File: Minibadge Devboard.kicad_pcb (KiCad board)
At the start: 2 copper layers, 30.5 x 48.3 mm, 39 parts, among them Q1 PMOS, SW1 Power, SW3 SPEED, SW4 NTC, U1 DRV8837C, U2 74HC4060

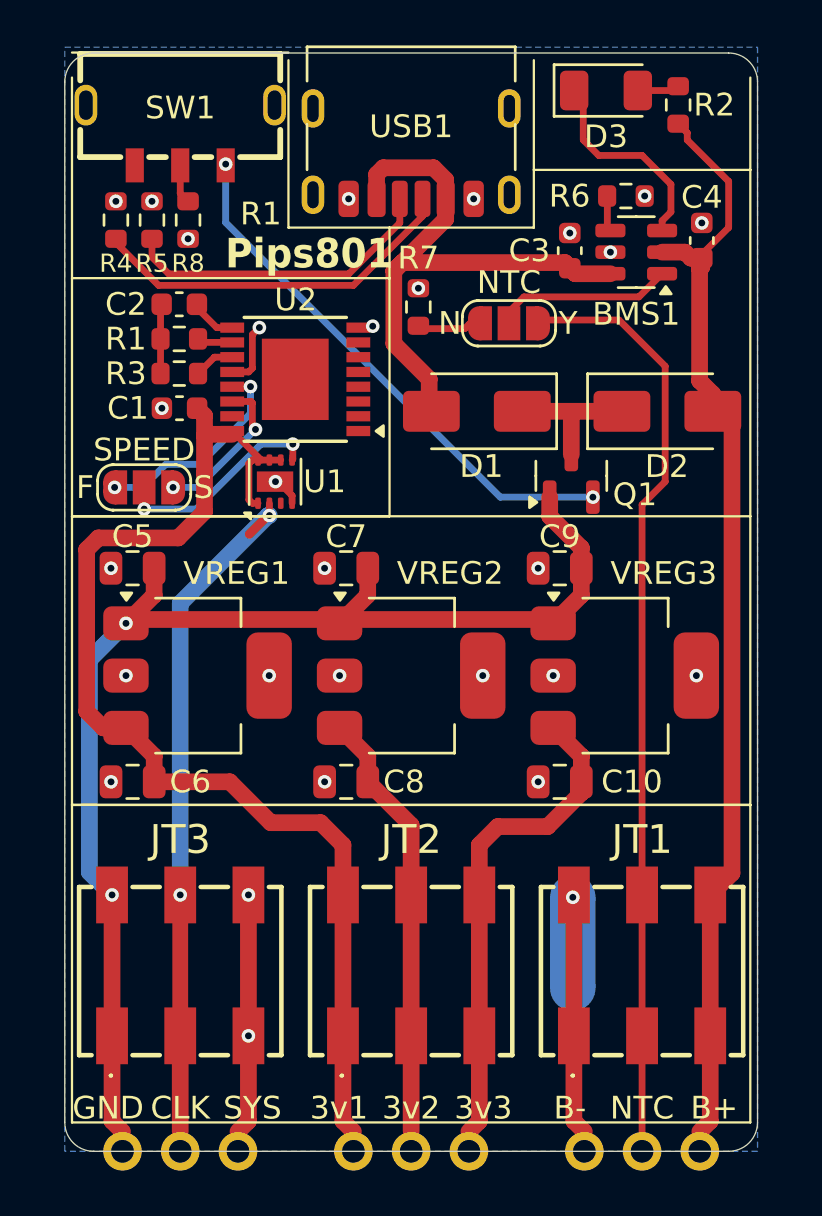
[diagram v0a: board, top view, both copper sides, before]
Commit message: Add Footprint and Symbol
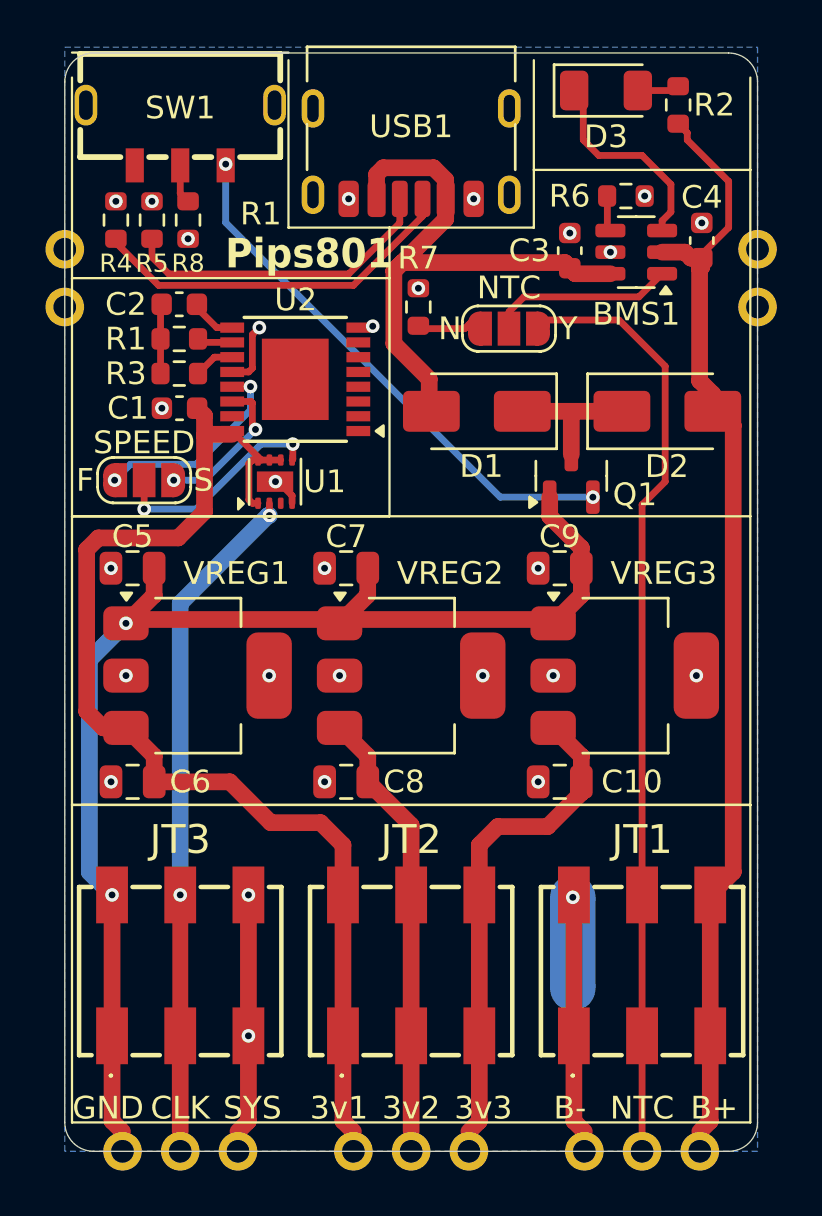
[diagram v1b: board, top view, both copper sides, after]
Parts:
- added G***: LOGO, LOGO, B.Cu at (178.8, 116.8)
- added REF**: Castellated pins 1x02, Castellated pins:Castellated pins 1x02, F.Cu at (195.6, 105.1)
- added REF**: Castellated pins 1x02, Castellated pins:Castellated pins 1x02, F.Cu at (165.1, 105.1)
- moved SW3 0.32 mm to (168.6, 112.7)
- moved SW4 0.24 mm to (184.6, 106.0)
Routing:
- net CLK: track 30.5 -> 29.4 mm

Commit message: Silkscreen fixes and thermal via stitching/anchoring
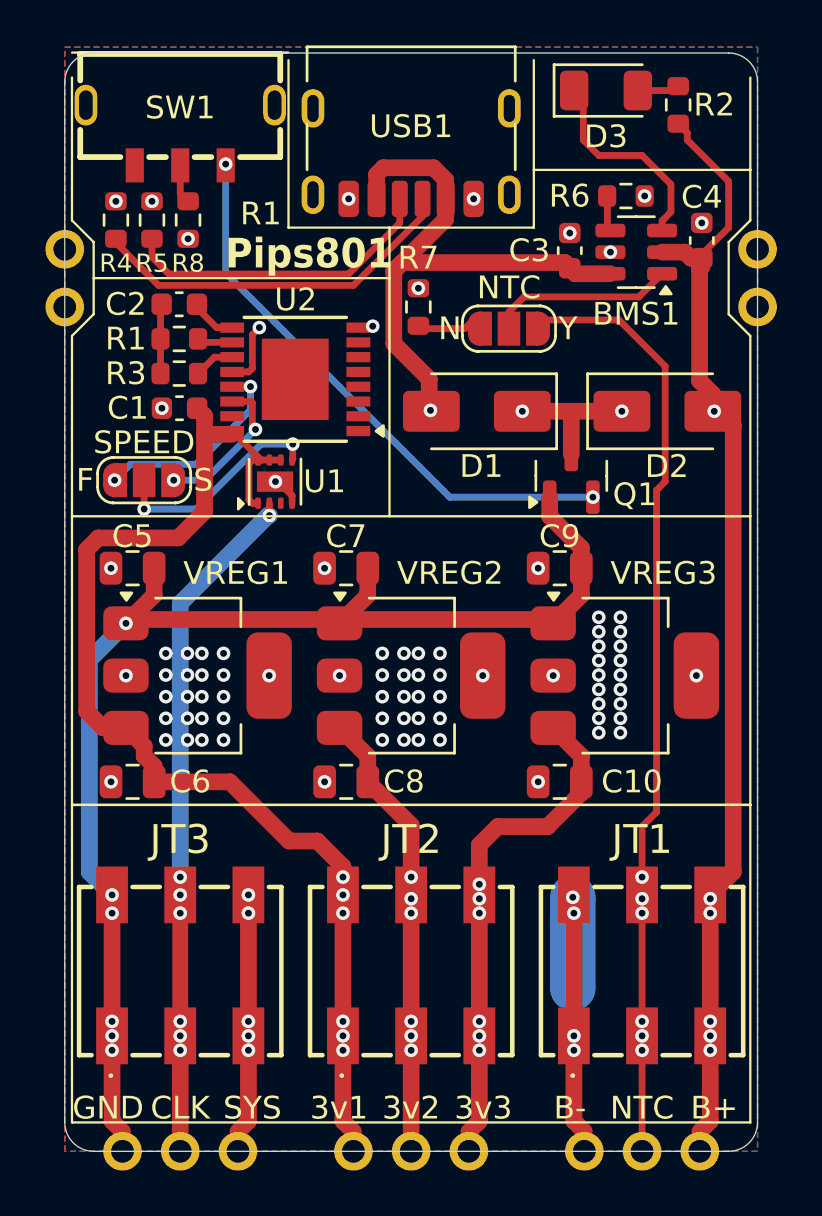
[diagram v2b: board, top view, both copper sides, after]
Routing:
- net Net-(Q1-G): track 23.7 -> 25.0 mm
- net +3.3V-1: track 51.3 -> 50.7 mm, vias 0 -> 6
- net VBUS: vias 0 -> 1
- net GND: vias 28 -> 89
- net VDD: vias 0 -> 2
- net SYS: vias 2 -> 6
- net NTC: vias 0 -> 6
- net CLK: vias 2 -> 7
- net -BATT: vias 1 -> 4
- net +BATT: vias 0 -> 6
- net +3.3V-3: vias 0 -> 6
- net +3.3V-2: vias 0 -> 6
- added copper zone on F.Cu, net GND

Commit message: Add support for external PSU and Power switch
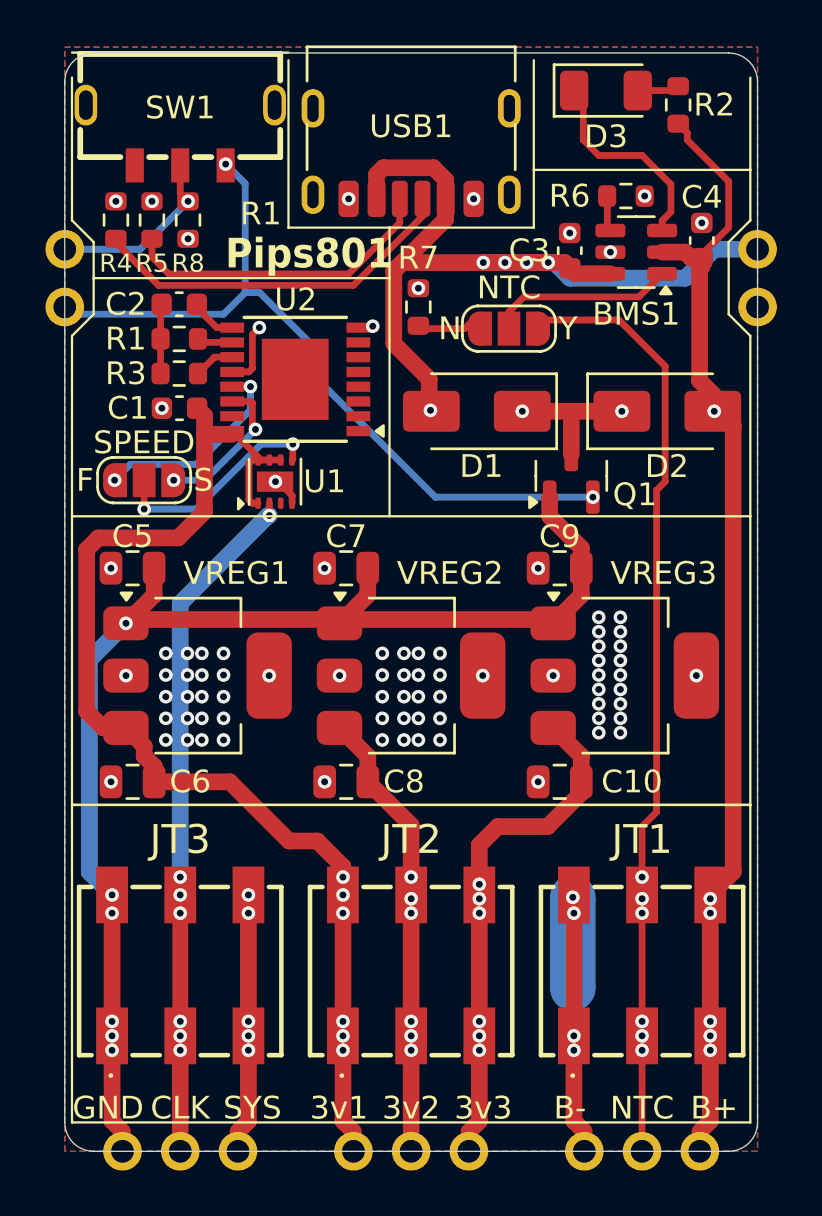
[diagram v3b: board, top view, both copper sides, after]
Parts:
- D3: value Charge -> RED
- J1: renamed from REF**; value Castellated pins 1x02 -> External power
- J2: renamed from REF**; value Castellated pins 1x02 -> External switch
- R1: value 8.45k -> 8.45kΩ
- R3: value 20k -> 20kΩ
- R4, R5: value 5.1k -> 5.1kΩ
- R6: value 675 -> 675Ω
- R7: value 10k -> 10kΩ
- R8: value 100k -> 100kΩ
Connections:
- J1 pad 1: (no net) -> GND
- J1 pad 2: (no net) -> VBUS
- J2 pad 1: (no net) -> SW1
- J2 pad 2: (no net) -> SW2
- Q1 pad 2: Net-(Q1-G) -> SW1
- R8 pad 1: Net-(SW1-B) -> SW2
- SW1 pad 1: Net-(Q1-G) -> SW1
- SW1 pad 2: Net-(SW1-B) -> SW2
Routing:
- net SW1: track 0.00 -> 34.2 mm, vias 0 -> 2
- net Net-(Q1-G): track 25.0 -> 0.00 mm, vias 2 -> 0
- net VBUS: track 26.2 -> 38.2 mm, vias 1 -> 5
- net SW2: track 0.00 -> 7.37 mm, vias 0 -> 1
- net Net-(SW1-B): track 1.72 -> 0.00 mm

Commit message: BOM updates
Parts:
- D3: footprint LED_SMD:LED_1206_3216Metric -> LED_SMD:LED_0603_1608Metric
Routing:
- net VBUS: track 38.2 -> 45.8 mm
- net CLK_LOW: track 9.71 -> 9.08 mm
- net Net-(D3-A): track 1.76 -> 2.37 mm
- net CLK: track 29.4 -> 29.9 mm
- net GND: vias 89 -> 79

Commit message: LCSC part numbers
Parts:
- R2: value R_CHG -> R_CHG 120-150Ω
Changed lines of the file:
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@@
 			)
 		)
+		(property "LCSC Part #" "C1779"
+			(at 0 0 0)
+			(unlocked yes)
+			(layer "F.Fab")
+			(hide yes)
+			(effects
+				(font
+					(size 1 1)
+					(thickness 0.15)
+				)
+			)
+		)
 		(property ki_fp_filters "C_*")
 		(sheetname "/")
@@
 			)
 		)
+		(property "LCSC Part #" "C15849"
+			(at 0 0 90)
+			(unlocked yes)
+			(layer "F.Fab")
+			(hide yes)
+			(effects
+				(font
+					(size 1 1)
+					(thickness 0.15)
+				)
+			)
+		)
 		(property ki_fp_filters "C_*")
 		(sheetname "/")
@@
 			)
 		)
-		(property "Value" "R_CHG"
+		(property "Value" "R_CHG 120-150Ω"
 			(at 0 1.43 90)
 			(layer "F.Fab")
@@
 			)
 		)
+		(property "LCSC Part #" ""
+			(at 0 0 90)
+			(unlocked yes)
+			(layer "F.Fab")
+			(hide yes)
+			(effects
+				(font
+					(size 1 1)
+					(thickness 0.15)
+				)
+			)
+		)
 		(property ki_fp_filters "R_*")
 		(sheetname "/")
@@
 			)
 		)
+		(property "LCSC Part #" "C14663"
+			(at 0 0 180)
+			(unlocked yes)
+			(layer "F.Fab")
+			(hide yes)
+			(effects
+				(font
+					(size 1 1)
+					(thickness 0.15)
+				)
+			)
+		)
 		(property ki_fp_filters "C_*")
 		(sheetname "/")
@@
 			)
 		)
+		(property "LCSC Part #" "C25981"
+			(at 0 0 0)
+			(unlocked yes)
+			(layer "F.Fab")
+			(hide yes)
+			(effects
+				(font
+					(size 1 1)
+					(thickness 0.15)
+				)
+			)
+		)
 		(property ki_fp_filters "R_*")
 		(sheetname "/")
@@
 			)
 		)
+		(property "LCSC Part #" "C1779"
+			(at 0 0 0)
+			(unlocked yes)
+			(layer "F.Fab")
+			(hide yes)
+			(effects
+				(font
+					(size 1 1)
+					(thickness 0.15)
+				)
+			)
+		)
 		(property ki_fp_filters "C_*")
 		(sheetname "/")
@@
 			)
 		)
+		(property "LCSC Part #" "C4184"
+			(at 0 0 0)
+			(unlocked yes)
+			(layer "F.Fab")
+			(hide yes)
+			(effects
+				(font
+					(size 1 1)
+					(thickness 0.15)
+				)
+			)
+		)
 		(property ki_fp_filters "R_*")
 		(sheetname "/")
@@
 			)
 		)
+		(property "LCSC Part #" "C1779"
+			(at 0 0 0)
+			(unlocked yes)
+			(layer "F.Fab")
+			(hide yes)
+			(effects
+				(font
+					(size 1 1)
+					(thickness 0.15)
+				)
+			)
+		)
 		(property ki_fp_filters "C_*")
 		(sheetname "/")
@@
 			)
 		)
+		(property "LCSC Part #" "C15849"
+			(at 0 0 90)
+			(unlocked yes)
+			(layer "F.Fab")
+			(hide yes)
+			(effects
+				(font
+					(size 1 1)
+					(thickness 0.15)
+				)
+			)
+		)
 		(property ki_fp_filters "C_*")
 		(sheetname "/")
@@
 			)
 		)
+		(property "LCSC Part #" "C23186"
+			(at 0 0 90)
+			(unlocked yes)
+			(layer "F.Fab")
+			(hide yes)
+			(effects
+				(font
+					(size 1 1)
+					(thickness 0.15)
+				)
+			)
+		)
 		(property ki_fp_filters "R_*")
 		(sheetname "/")
@@
 			)
 		)
-		(property "LCSC Part #" "C3743528"
+		(property "LCSC Part #" "C500795"
 			(at 0 0 0)
 			(unlocked yes)
@@
 			)
 		)
+		(property "LCSC Part #" "C23228"
+			(at 0 0 0)
+			(unlocked yes)
+			(layer "F.Fab")
+			(hide yes)
+			(effects
+				(font
+					(size 1 1)
+					(thickness 0.15)
+				)
+			)
+		)
 		(property ki_fp_filters "R_*")
 		(sheetname "/")
@@
 			)
 		)
+		(property "LCSC Part #" "C25803"
+			(at 0 0 270)
+			(unlocked yes)
+			(layer "F.Fab")
+			(hide yes)
+			(effects
+				(font
+					(size 1 1)
+					(thickness 0.15)
+				)
+			)
+		)
 		(property ki_fp_filters "R_*")
 		(sheetname "/")
@@
 			)
 		)
+		(property "LCSC Part #" "C1779"
+			(at 0 0 0)
+			(unlocked yes)
+			(layer "F.Fab")
+			(hide yes)
+			(effects
+				(font
+					(size 1 1)
+					(thickness 0.15)
+				)
+			)
+		)
 		(property ki_fp_filters "C_*")
 		(sheetname "/")
@@
 			)
 		)
-		(property "LCSC Part #" "C3743528"
+		(property "LCSC Part #" "C500795"
 			(at 0 0 0)
 			(unlocked yes)
@@
 			)
 		)
-		(property "LCSC Part #" "C3743528"
+		(property "LCSC Part #" "C500795"
 			(at 0 0 0)
 			(unlocked yes)
@@
 			)
 		)
+		(property "LCSC Part #" "C1779"
+			(at 0 0 0)
+			(unlocked yes)
+			(layer "F.Fab")
+			(hide yes)
+			(effects
+				(font
+					(size 1 1)
+					(thickness 0.15)
+				)
+			)
+		)
 		(property ki_fp_filters "C_*")
 		(sheetname "/")
@@
 			)
 		)
+		(property "LCSC Part #" "C1779"
+			(at 0 0 0)
+			(unlocked yes)
+			(layer "F.Fab")
+			(hide yes)
+			(effects
+				(font
+					(size 1 1)
+					(thickness 0.15)
+				)
+			)
+		)
 		(property ki_fp_filters "C_*")
 		(sheetname "/")
@@
 			)
 		)
+		(property "LCSC Part #" "C23186"
+			(at 0 0 90)
+			(unlocked yes)
+			(layer "F.Fab")
+			(hide yes)
+			(effects
+				(font
+					(size 1 1)
+					(thickness 0.15)
+				)
+			)
+		)
 		(property ki_fp_filters "R_*")
 		(sheetname "/")
@@
 			)
 		)
+		(property "LCSC Part #" "C25804"
+			(at 0 0 90)
+			(unlocked yes)
+			(layer "F.Fab")
+			(hide yes)
+			(effects
+				(font
+					(size 1 1)
+					(thickness 0.15)
+				)
+			)
+		)
 		(property ki_fp_filters "R_*")
 		(sheetname "/")
@@
 					(thickness 0.15)
 				)
+			)
+		)
+		(property "LCSC Part #" "C14663"
+			(at 0 0 0)
+			(unlocked yes)
+			(layer "F.Fab")
+			(hide yes)
+			(effects
+				(font
+					(size 1 1)
+					(thickness 0.15)
+				)

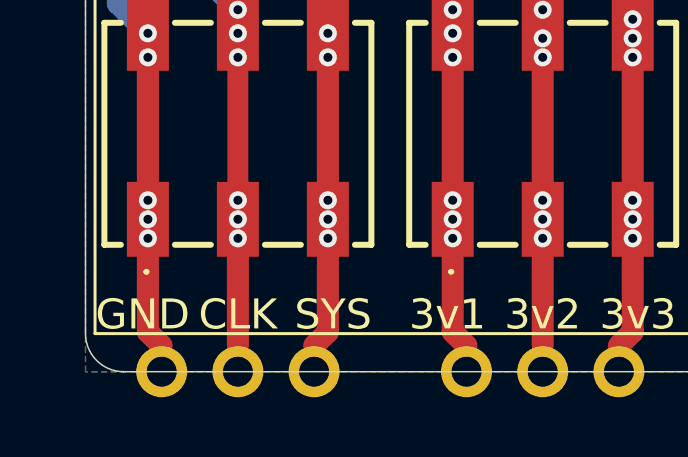
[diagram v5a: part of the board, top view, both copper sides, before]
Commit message: Fixes
* Added text to the footprint to clarify which castellated pin is what
* Fixed pinout issue with footprint and symbol. SYS and GND were reversed (yikes)
* Updated schematic symbols and values
* push updated schematic PDF
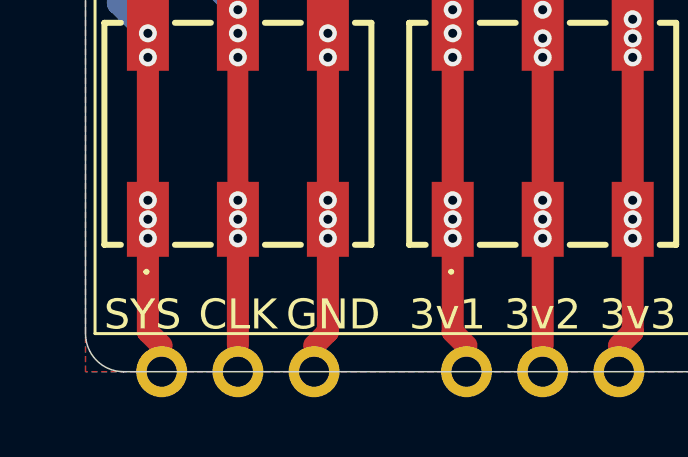
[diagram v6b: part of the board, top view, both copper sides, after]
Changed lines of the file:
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@@
 		)
 	)
-	(gr_text "GND"
+	(gr_text "SYS"
 		(at 167.005 140.335 0)
 		(layer "F.SilkS" knockout)
@@
 		)
 	)
-	(gr_text "SYS"
+	(gr_text "GND"
 		(at 173.355 140.335 0)
 		(layer "F.SilkS" knockout)
